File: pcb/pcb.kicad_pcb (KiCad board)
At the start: 2 copper layers, 217.1 x 70.2 mm, 97 parts, among them SW1 SW_SPST, SW10 SW_SPST, SW11 SW_SPST, SW12 SW_SPST, SW13 SW_SPST, SW14 SW_SPST, SW15 SW_SPST, SW16 SW_SPST, SW17 SW_SPST, SW18 SW_SPST, SW19 SW_SPST, SW2 SW_SPST, SW20 SW_SPST, SW21 SW_SPST, SW22 SW_SPST, SW23 SW_SPST, SW24 SW_SPST, SW25 SW_SPST, SW26 SW_SPST, SW27 SW_SPST, SW28 SW_SPST, SW29 SW_SPST, SW3 SW_SPST, SW30 SW_SPST, SW31 SW_SPST, SW32 SW_SPST, SW33 SW_SPST, SW34 SW_SPST, SW35 SW_SPST, SW36 SW_SPST, SW37 SW_SPST, SW38 SW_SPST, SW39 SW_SPST, SW4 SW_SPST, SW40 SW_SPST, SW41 SW_SPST, SW42 SW_SPST, SW43 SW_SPST, SW44 SW_SPST, SW45 SW_SPST, SW46 SW_SPST, SW47 SW_SPST, SW48 SW_SPST, SW5 SW_SPST, SW6 SW_SPST, SW7 SW_SPST, SW8 SW_SPST, SW9 SW_SPST, U1 SuperMini nRF52840

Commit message: pcb v1 done
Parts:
- added SW49: SW_SPST, TS-1088-AR02016:SW_TS-1088-AR02016, B.Cu at (240.7, 73.7)
- D1, D10, D11, D12, D13, D14, D15, D16, D17, D18, D19, D2, D20, D21, D22, D23, D24, D25, D26, D27, D28, D29, D3, D30, D31, D32, D33, D34, D35, D36, D37, D38, D39, D4, D40, D41, D42, D43, D44, D45, D46, D47, D48, D5, D6, D7, D8, D9: moved to B.Cu
- U1: footprint PCM_marbastlib-xp-promicroish:SuperMini_nRF52840_AH_USBdn -> PCM_marbastlib-xp-promicroish:SuperMini_nRF52840_H_USBdn; moved to B.Cu
- moved U1 90.1 mm to (234.0, 43.6), turned to 180 degrees
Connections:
- U1 pad 10: unconnected-(U1-P0.11-Pad10) -> col5
- U1 pad 11: unconnected-(U1-P1.04-LF-Pad11) -> col6
- U1 pad 12: unconnected-(U1-P1.06-LF-Pad12) -> col7
- U1 pad 14: unconnected-(U1-GND-Pad14) -> GND
- U1 pad 15: unconnected-(U1-RST-Pad15) -> Net-(SW49-A)
- U1 pad 17: unconnected-(U1-P0.31-LF-Pad17) -> row0
- U1 pad 18: unconnected-(U1-P0.29-LF-Pad18) -> row1
- U1 pad 19: unconnected-(U1-P0.02-LF-Pad19) -> col11
- U1 pad 20: unconnected-(U1-P1.15-LF-Pad20) -> col10
- U1 pad 21: unconnected-(U1-P1.13-LF-Pad21) -> col9
- U1 pad 22: unconnected-(U1-P1.11-LF-Pad22) -> col8
- U1 pad 23: unconnected-(U1-P0.10-LF-Pad23) -> row2
- U1 pad 24: unconnected-(U1-P0.09-LF-Pad24) -> row3
- U1 pad 3: unconnected-(U1-GND-Pad3) -> GND
- U1 pad 4: unconnected-(U1-GND-Pad4) -> GND
- U1 pad 5: unconnected-(U1-P0.17-Pad5) -> col0
- U1 pad 6: unconnected-(U1-P0.20-Pad6) -> col1
- U1 pad 7: unconnected-(U1-P0.22-Pad7) -> col2
- U1 pad 8: unconnected-(U1-P0.24-Pad8) -> col3
- U1 pad 9: unconnected-(U1-P1.00-Pad9) -> col4
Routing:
- net col0: track 0.00 -> 258.9 mm
- net col1: track 0.00 -> 241.6 mm
- net row3: track 0.00 -> 232.8 mm
- net col2: track 0.00 -> 224.1 mm
- net row0: track 0.00 -> 224.1 mm
- net row2: track 0.00 -> 218.9 mm
- net row1: track 0.00 -> 217.2 mm
- net col3: track 0.00 -> 208.2 mm
- net col4: track 0.00 -> 193.1 mm
- net col5: track 0.00 -> 172.5 mm
- net col6: track 0.00 -> 153.5 mm
- net col7: track 0.00 -> 135.8 mm
- net col8: track 0.00 -> 126.3 mm
- net col9: track 0.00 -> 108.8 mm
- net col10: track 0.00 -> 92.8 mm
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
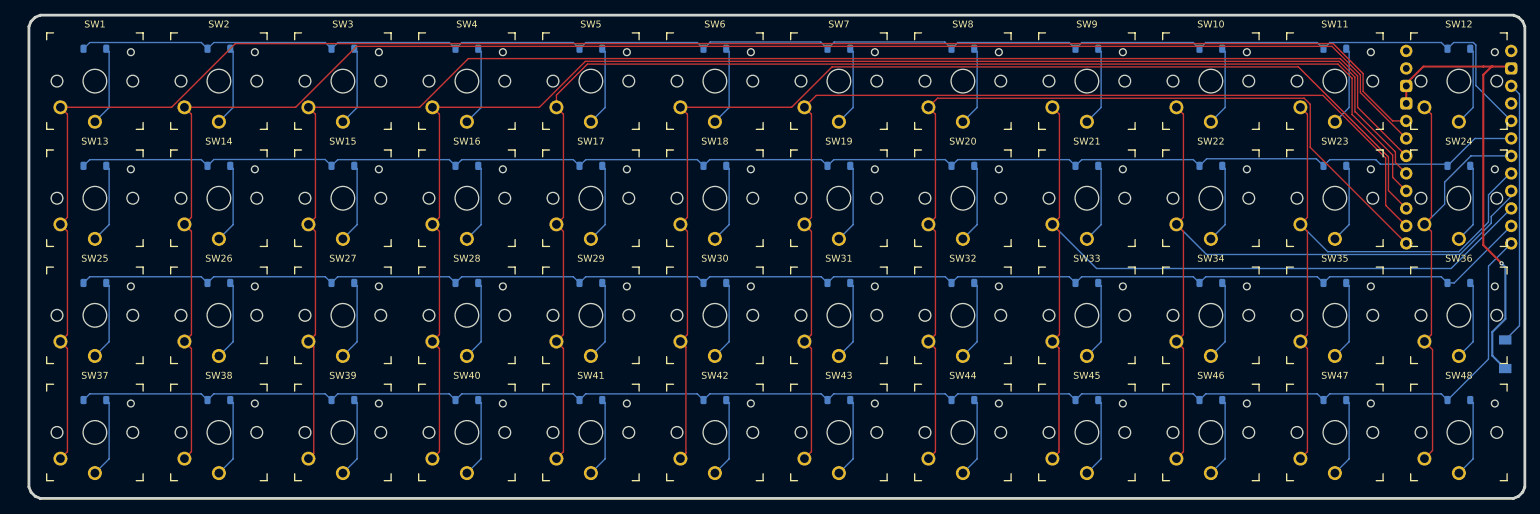
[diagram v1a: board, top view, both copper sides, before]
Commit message: firmware completed & CFX spacing
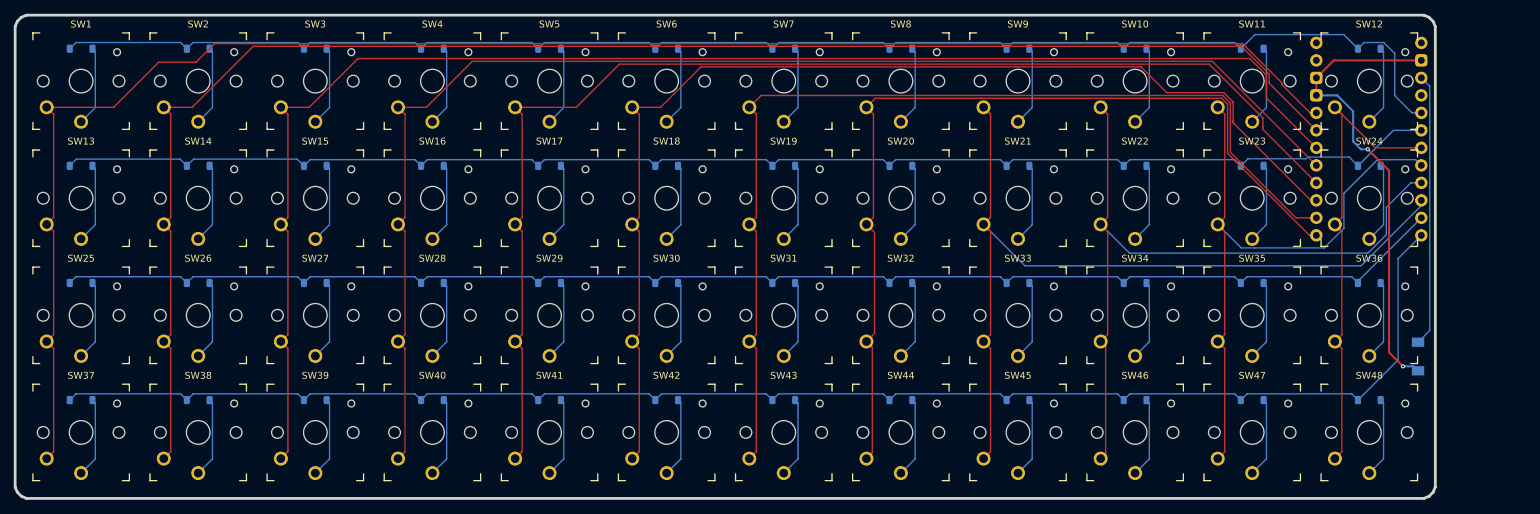
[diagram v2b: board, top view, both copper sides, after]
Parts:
- moved U1 13.1 mm to (220.9, 42.4)
- moved D12 13.0 mm to (221.0, 29.3)
- moved D24 13.0 mm to (221.0, 46.3)
- moved D36 13.0 mm to (221.0, 63.3)
- moved D48 13.0 mm to (221.0, 80.3)
- moved SW12 13.0 mm to (221.0, 34.0)
- moved SW24 13.0 mm to (221.0, 51.0)
- moved SW36 13.0 mm to (221.0, 68.0)
- moved SW48 13.0 mm to (221.0, 85.0)
- moved SW49 12.7 mm to (228.1, 74.0)
- moved D11 12.0 mm to (204.0, 29.3)
- moved D23 12.0 mm to (204.0, 46.3)
- moved D35 12.0 mm to (204.0, 63.3)
- moved D47 12.0 mm to (204.0, 80.3)
- moved SW11 12.0 mm to (204.0, 34.0)
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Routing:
- net col0: track 258.9 -> 246.0 mm
- net col4: track 193.1 -> 180.5 mm
- net col3: track 208.2 -> 195.9 mm
- net col1: track 241.6 -> 230.3 mm
- net row0: track 224.1 -> 213.5 mm
- net row2: track 218.9 -> 208.5 mm
- net row1: track 217.2 -> 207.0 mm
- net col2: track 224.1 -> 214.1 mm
- net row3: track 232.8 -> 222.9 mm
- net col5: track 172.5 -> 165.0 mm
- net col6: track 153.5 -> 148.1 mm
- net col7: track 135.8 -> 131.8 mm
- net col11: track 72.2 -> 68.6 mm
- net col8: track 126.3 -> 123.9 mm
- net GND: track 66.6 -> 68.2 mm, vias 1 -> 2
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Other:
- board size 217.1 x 70.2 mm -> 206.1 x 70.2 mm

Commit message: holes and cases
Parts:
- added H1: MountingHole, MountingHole:MountingHole_2.2mm_M2, F.Cu at (42.5, 42.5)
- added H2: MountingHole, MountingHole:MountingHole_2.2mm_M2, F.Cu at (42.5, 76.5)
- added H3: MountingHole, MountingHole:MountingHole_2.2mm_M2, F.Cu at (212.5, 76.5)
- added H4: MountingHole, MountingHole:MountingHole_2.2mm_M2, F.Cu at (195.5, 42.5)

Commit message: render, bom, finishing touches'
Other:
- board text added: "made w/ love by @wenbang24"
